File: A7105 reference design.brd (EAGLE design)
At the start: 14.7 x 11.8 mm, 38 parts, among them J1 JST-SH-3, SW1 BUTTON, U1 A7105, U2 ATTINY167, U3 NMOS, X1 ECX-2236

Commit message: Finished integrated rev 0.2
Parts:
- removed J1: JST-SH-3, nikdavis:JST-SH-3
- removed U$3, U$4: TESTPAD, AlienWhoop:TESTPAD
- added C19: 1uF, Perfect_0402:0402
- added U$10, U$11, U$12, U$6, U$7, U$8, U$9: TESTPAD, AlienWhoop:TESTPAD
- U3: value NMOS -> NMOSSOT833B/1006; device nikdavis:SOT23-3 -> nikdavis:SOT833B/DFN1006B-3
- moved R6 109.7 mm to (9.56, 3.17), flipped to the bottom, turned to 270 degrees
- moved C18 106.0 mm to (5.71, 7.90), flipped to the bottom
- moved R4 9.19 mm to (11.5, 10.7), turned to 180 degrees
- moved U3 3.90 mm to (14.0, 3.89)
- moved C11 2.54 mm to (8.87, 1.52), turned to 270 degrees
- moved R2 2.24 mm to (11.5, 5.47), turned to 90 degrees
- moved R3 2.10 mm to (9.92, 1.52), flipped to the top
- moved C1 1.95 mm to (5.66, 3.12), turned to 0 degrees
- moved SW1 1.86 mm to (11.0, 7.02), turned to 90 degrees
- moved C6 1.82 mm to (5.71, 4.02), turned to 0 degrees
- moved C10 1.64 mm to (4.95, 1.50), turned to 90 degrees
- moved U$5 1.00 mm to (7.24, 9.86)
- moved U2 1.00 mm to (10.4, 6.80)
- moved X1 0.64 mm to (5.46, 0.36)
- moved C14 0.58 mm to (0.85, 8.69)
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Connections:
- new net GPIO1: U1.16, U2.29
- net G: now also U3.P$1; no longer U3.1
- net GND: now also C19.2, U$9.TP, U3.P$2; no longer J1.2, J1.GND1, J1.GND2, U$4.TP, U3.2
- net MOSI: now also U$12.TP
- net RESET: now also U$7.TP
- net SBUS: now also U$6.TP, U3.P$3; no longer J1.3, U3.3
- net SCK: now also U$10.TP
- net SDIO: now also U$11.TP
- net VCC: now also C19.1, U$8.TP; no longer J1.1, U$3.TP
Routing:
- net SBUS_NONINV: track 11.7 -> 1.66 mm, vias 2 -> 0
- net G: track 1.30 -> 10.2 mm
- net SDIO: track 19.6 -> 11.6 mm
- net GPIO1: track 0.00 -> 7.85 mm, vias 0 -> 1
- net RESET: track 0.00 -> 6.47 mm, vias 0 -> 1
- net MOSI: track 1.15 -> 6.55 mm
- net GND: track 14.3 -> 10.6 mm, vias 18 -> 22
- net SCK: track 6.85 -> 10.2 mm
- net N$4: track 1.41 -> 3.94 mm
- net BIND: track 2.61 -> 4.94 mm
- net VCCA: track 13.2 -> 15.0 mm
- net AVRCLK: track 4.58 -> 3.30 mm
- net N$10: track 5.38 -> 4.27 mm
- net N$8: track 2.90 -> 3.96 mm
- net SCS: track 5.79 -> 4.91 mm
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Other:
- board size 14.7 x 11.8 mm -> 15 x 11.5 mm

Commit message: Cleanup before order
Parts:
- moved R5 0.56 mm to (7.65, 10.4)
- moved U$5 0.53 mm to (7.24, 10.4)
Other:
- board text added: "3.3"
- board text added: "G"
- board text added: "MI"
- board text added: "MO"
- board text added: "RST"
- board text added: "SB"
- board text added: "SCK"
- board text added: "uFlSky SBUS @nivvis V0.2"
- board text removed: "A7105 Ref Integrated V0.1 / 2019-02-16 nivvis"
- board text removed: "GND"
- board text removed: "VCC"

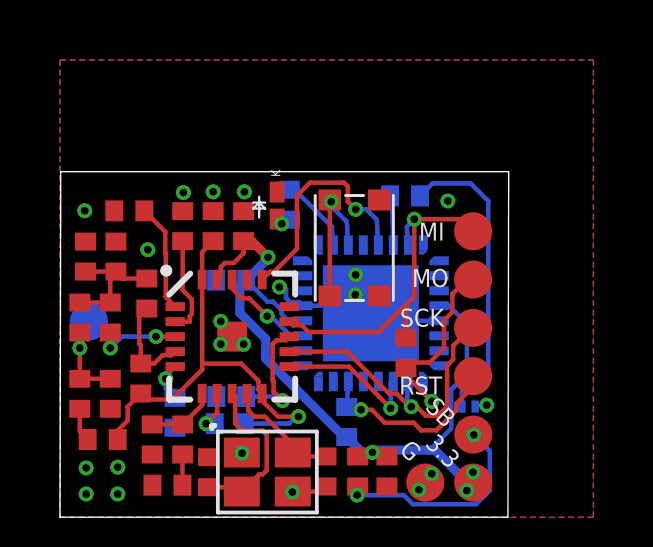
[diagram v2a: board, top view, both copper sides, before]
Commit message: Add bind pull up
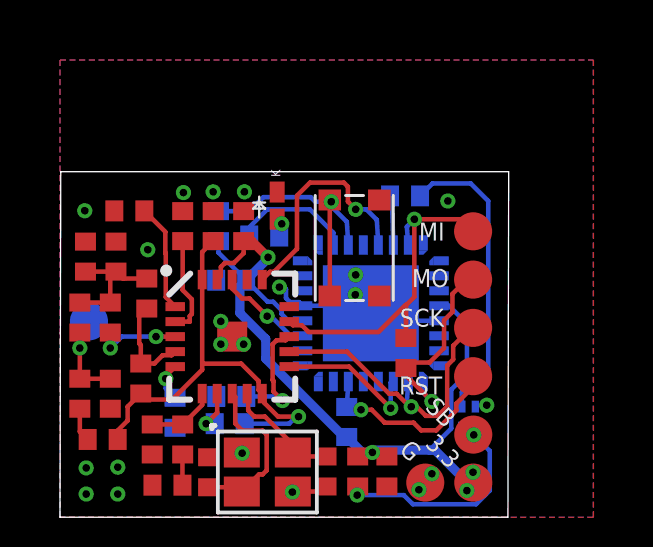
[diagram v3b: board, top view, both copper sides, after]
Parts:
- added R7: 10k, Perfect_0402:0402
- moved R5 1.34 mm to (6.81, 9.37), turned to 180 degrees
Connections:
- net BIND: now also R7.1
- net VCC: now also R7.2
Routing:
- net BIND: track 4.94 -> 8.95 mm
- net VCC: track 26.4 -> 28.0 mm
- net STATUS: track 2.54 -> 4.07 mm
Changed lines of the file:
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@@
 <setting verticaltext="up"/>
 </settings>
-<grid distance="0.001" unitdist="inch" unit="mm" style="lines" multiple="1" display="no" altdistance="5" altunitdist="mil" altunit="mil"/>
+<grid distance="0.001" unitdist="inch" unit="inch" style="lines" multiple="1" display="no" altdistance="5" altunitdist="mil" altunit="mil"/>
 <layers>
 <layer number="1" name="Top" color="4" fill="1" visible="yes" active="yes"/>
-<layer number="16" name="Bottom" color="1" fill="1" visible="no" active="yes"/>
-<layer number="17" name="Pads" color="2" fill="1" visible="no" active="yes"/>
-<layer number="18" name="Vias" color="2" fill="1" visible="no" active="yes"/>
-<layer number="19" name="Unrouted" color="6" fill="1" visible="no" active="yes"/>
-<layer number="20" name="Dimension" color="24" fill="1" visible="no" active="yes"/>
+<layer number="16" name="Bottom" color="1" fill="1" visible="yes" active="yes"/>
+<layer number="17" name="Pads" color="2" fill="1" visible="yes" active="yes"/>
+<layer number="18" name="Vias" color="2" fill="1" visible="yes" active="yes"/>
+<layer number="19" name="Unrouted" color="6" fill="1" visible="yes" active="yes"/>
+<layer number="20" name="Dimension" color="24" fill="1" visible="yes" active="yes"/>
 <layer number="21" name="tPlace" color="7" fill="1" visible="yes" active="yes"/>
-<layer number="22" name="bPlace" color="7" fill="1" visible="no" active="yes"/>
-<layer number="23" name="tOrigins" color="15" fill="1" visible="no" active="yes"/>
-<layer number="24" name="bOrigins" color="15" fill="1" visible="no" active="yes"/>
+<layer number="22" name="bPlace" color="7" fill="1" visible="yes" active="yes"/>
+<layer number="23" name="tOrigins" color="15" fill="1" visible="yes" active="yes"/>
+<layer number="24" name="bOrigins" color="15" fill="1" visible="yes" active="yes"/>
 <layer number="25" name="tNames" color="7" fill="1" visible="no" active="yes"/>
 <layer number="26" name="bNames" color="7" fill="1" visible="no" active="yes"/>
@@
 <element name="R4" library="Perfect_0402" package="0402" value="10k" x="11.5018" y="10.7102" smashed="yes" rot="MR180"/>
 <element name="SW1" library="nikdavis" package="PTS-830-SMD-SWITCH" value="BUTTON" x="11.0174" y="7.0238" smashed="yes" rot="R90"/>
-<element name="R5" library="Perfect_0402" package="0402" value="200" x="7.6454" y="10.414" smashed="yes" rot="MR270"/>
+<element name="R5" library="Perfect_0402" package="0402" value="200" x="6.8072" y="9.3726" smashed="yes" rot="MR180"/>
 <element name="U$5" library="alienflight" package="0402LED" value="SMD-CHIP-LED-0402" x="7.239" y="10.3886" smashed="yes" rot="R270"/>
 <element name="C18" library="Perfect_0402" package="0402" value="10nF" x="5.7052" y="7.8982" smashed="yes" rot="MR0">
@@
 <attribute name="DNP" value="T" x="13.77" y="7.92" size="1.778" layer="27" display="off"/>
 <attribute name="VALUE" x="13.135" y="7.158" size="0.0254" layer="27"/>
+</element>
+<element name="R7" library="Perfect_0402" package="0402" value="10k" x="5.2832" y="9.7028" smashed="yes" rot="MR270">
+<attribute name="NAME" x="4.7482" y="10.3378" size="0.8128" layer="26" ratio="10" rot="MR270"/>
+<attribute name="VALUE" x="6.6882" y="10.3378" size="0.8128" layer="28" ratio="10" rot="MR270"/>
 </element>
 </elements>
@@
 <wire x1="13.7754" y1="1.1532" x2="13.7754" y2="1.49" width="0.3048" layer="1"/>
 <wire x1="13.7754" y1="1.49" x2="13.7668" y2="1.4986" width="0.3048" layer="1"/>
+<contactref element="R7" pad="2"/>
+<wire x1="5.2832" y1="9.2028" x2="5.2832" y2="8.8202" width="0.1524" layer="16"/>
+<wire x1="5.2832" y1="8.8202" x2="6.2052" y2="7.8982" width="0.1524" layer="16"/>
 </signal>
 <signal name="N$8">
@@
 <wire x1="9.0424" y1="10.5238" x2="9.0424" y2="10.5156" width="0.1524" layer="1"/>
 <wire x1="8.9924" y1="10.5738" x2="8.9924" y2="7.3738" width="0.1524" layer="1"/>
+<contactref element="R7" pad="1"/>
+<wire x1="9.0424" y1="10.5156" x2="8.50825625" y2="10.5156" width="0.1524" layer="16"/>
+<wire x1="8.50825625" y1="10.5156" x2="8.35585625" y2="10.668" width="0.1524" layer="16"/>
+<wire x1="8.35585625" y1="10.668" x2="6.7818" y2="10.668" width="0.1524" layer="16"/>
+<wire x1="6.7818" y1="10.668" x2="6.3166" y2="10.2028" width="0.1524" layer="16"/>
+<wire x1="6.3166" y1="10.2028" x2="5.2832" y2="10.2028" width="0.1524" layer="16"/>
 </signal>
 <signal name="RESET">
@@
 <contactref element="U2" pad="26"/>
 <contactref element="R5" pad="1"/>
-<wire x1="9.1116" y1="9.0726" x2="9.0608" y2="9.6804" width="0.1524" layer="16"/>
-<wire x1="9.0608" y1="9.6804" x2="7.8272" y2="10.914" width="0.1524" layer="16"/>
-<wire x1="7.8272" y1="10.914" x2="7.6454" y2="10.914" width="0.1524" layer="16"/>
+<wire x1="9.1116" y1="9.0726" x2="9.1116" y2="9.4812" width="0.1524" layer="16"/>
+<wire x1="8.3312" y1="10.2616" x2="6.9088" y2="10.2616" width="0.1524" layer="16"/>
+<wire x1="6.9088" y1="10.2616" x2="6.3072" y2="9.66" width="0.1524" layer="16"/>
+<wire x1="6.3072" y1="9.66" x2="6.3072" y2="9.3726" width="0.1524" layer="16"/>
+<wire x1="9.1116" y1="9.4812" x2="8.3312" y2="10.2616" width="0.1524" layer="16"/>
 </signal>
 <signal name="N$9">
@@
 <contactref element="U$5" pad="2"/>
 <via x="7.3914" y="9.779" extent="1-16" drill="0.254"/>
-<wire x1="7.6454" y1="9.914" x2="7.5104" y2="9.779" width="0.1524" layer="16"/>
-<wire x1="7.3914" y1="9.779" x2="7.5104" y2="9.779" width="0.1524" layer="16"/>
+<wire x1="7.3914" y1="9.779" x2="7.3072" y2="9.6948" width="0.1524" layer="16"/>
+<wire x1="7.3072" y1="9.6948" x2="7.3072" y2="9.3726" width="0.1524" layer="16"/>
 <wire x1="7.239" y1="9.9386" x2="7.3914" y2="9.7862" width="0.1524" layer="1"/>
 <wire x1="7.3914" y1="9.7862" x2="7.3914" y2="9.779" width="0.1524" layer="1"/>

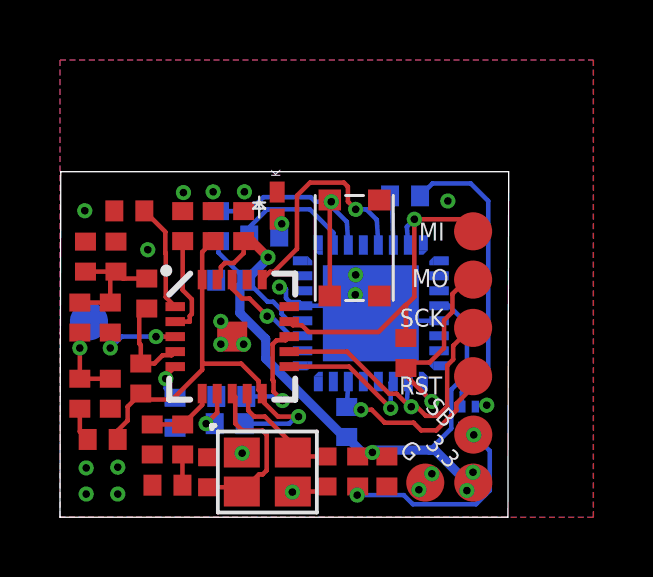
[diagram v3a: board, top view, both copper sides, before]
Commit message: Start STM rehaul -- stuck on EEPROM decision
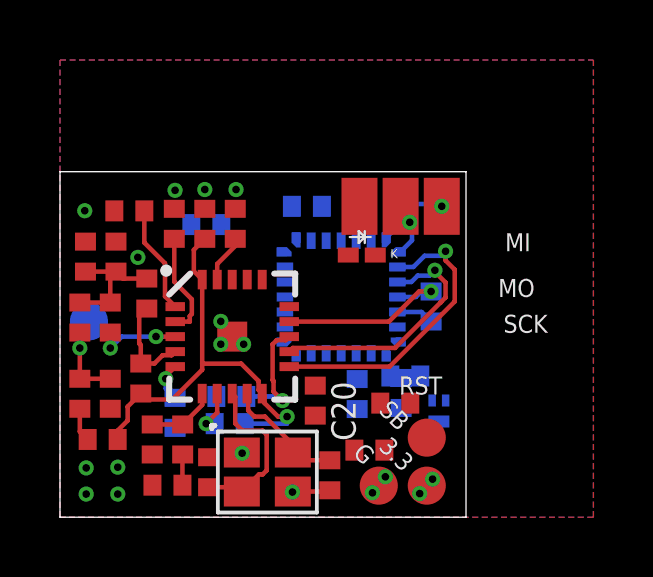
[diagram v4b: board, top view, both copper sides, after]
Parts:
- removed R7: 10k, Perfect_0402:0402
- removed SW1: BUTTON, nikdavis:PTS-830-SMD-SWITCH
- removed U$10, U$11, U$12, U$7: TESTPAD, AlienWhoop:TESTPAD
- added C20, C21: 10nF, Perfect_0402:0402
- added TP1, TP2, TP3: TESTPAD, nikdavis:SMTPAD-RECT
- R6: value 4k7 -> 10k
- U2: value ATTINY167 -> STM32F031G4U6; device nikdavis:VQFN-32 -> STM32F031G4U6:QFN50P400X400X60-28N
- moved R4 6.00 mm to (11.5, 4.71), turned to 0 degrees
- moved C18 5.66 mm to (9.91, 4.11), turned to 270 degrees
- moved U$5 3.27 mm to (10.1, 8.74), turned to 180 degrees
- moved R3 2.60 mm to (11.2, 3.80), turned to 180 degrees
- moved R6 2.06 mm to (11.4, 4.14), turned to 90 degrees
- moved R5 1.97 mm to (4.88, 9.75)
- moved R2 1.76 mm to (12.4, 7.02), flipped to the bottom
- moved U$9 1.55 mm to (10.6, 1.05)
- moved U$6 1.55 mm to (12.2, 2.65)
- moved U$8 1.55 mm to (12.2, 1.05)
- moved U2 1.13 mm to (9.37, 7.34), turned to 90 degrees
- moved U3 1.01 mm to (13.0, 4.09)
- moved C19 0.92 mm to (10.3, 2.24), turned to 180 degrees
- moved C5 0.29 mm to (4.83, 9.78)
- moved C9 0.29 mm to (5.84, 9.78)
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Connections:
- removed net AVRCLK: U1.18, U2.19
- removed net BIND: R7.1, SW1.P$1, SW1.P$2, U2.27
- removed net RESET: R6.1, U$7.TP, U2.14
- removed net SBUS_NONINV: R4.1, U2.30
- new net MCUCLK: U1.18
- new net N$11: C18.1, U2.4
- new net N$5: R6.2, U2.1
- new net NSBUS: R4.1, U2.27
- new net SWCLK: TP2.P$1, U2.22
- new net SWD: TP1.P$1, U2.21
- net GND: now also C20.2, C21.2, R6.1, TP3.P$1, U2.16; no longer SW1.P$3, SW1.P$4, U2.21, U2.5, U2.PAD
- net GPIO1: now also U2.20; no longer U2.29
- net MOSI: now also U2.26; no longer U$12.TP, U2.9
- net SCK: now also U2.24; no longer U$10.TP, U2.10
- net SCS: now also U2.23; no longer U2.11
- net SDIO: now also U2.25; no longer U$11.TP, U2.31
- net STATUS: no longer U2.26
- net VCC: now also C20.1, C21.1, U2.17, U2.5; no longer C18.1, R6.2, R7.2, U2.20, U2.4
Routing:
- net VCC: track 28.0 -> 1.61 mm, vias 4 -> 0
- net G: track 10.2 -> 0.00 mm
- net BIND: track 8.95 -> 0.00 mm, vias 1 -> 0
- net GPIO1: track 7.85 -> 0.00 mm, vias 1 -> 0
- net SBUS: track 7.44 -> 0.00 mm, vias 2 -> 0
- net GND: track 10.6 -> 3.82 mm, vias 22 -> 17
- net RESET: track 6.47 -> 0.00 mm, vias 1 -> 0
- net MOSI: track 6.55 -> 1.25 mm, vias 1 -> 0
- net SDIO: track 11.6 -> 6.34 mm
- net SCS: track 4.91 -> 10.0 mm
- net STATUS: track 4.07 -> 0.00 mm
- net AVRCLK: track 3.30 -> 0.00 mm, vias 1 -> 0
- net SWD: track 0.00 -> 2.62 mm, vias 0 -> 1
- net SWCLK: track 0.00 -> 1.86 mm, vias 0 -> 1
- net SCK: track 10.2 -> 8.43 mm
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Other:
- board size 15 x 11.5 mm -> 13.5 x 11.5 mm

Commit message: Small edits
Bit of board prep organization. Small schematic clean up and notes.
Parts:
- removed C21: 10nF, Perfect_0402:0402
- C20: value 10nF -> 0.1uF
- moved C20 6.32 mm to (7.98, 10.2), flipped to the bottom, turned to 0 degrees
- moved U$5 2.74 mm to (7.80, 10.3)
- moved R4 1.00 mm to (12.4, 5.22), turned to 270 degrees
- moved R5 0.84 mm to (5.64, 10.1)
- moved R3 0.47 mm to (10.8, 3.56), turned to 270 degrees
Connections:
- net GND: no longer C21.2
- net VCC: no longer C21.1

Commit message: First steps
Remove inverter
Make todo list
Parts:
- removed R3, R4: 10k, Perfect_0402:0402
- removed U3: NMOSSOT833B/1006, nikdavis:SOT833B/DFN1006B-3
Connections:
- removed net G: R4.2, U3.P$1
- removed net NSBUS: R4.1, U2.27
- net GND: no longer U3.P$2
- net SBUS: now also U2.27; no longer R3.1, U3.P$3
- net VCC: no longer R3.2
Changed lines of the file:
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@@
 <element name="X1" library="nikdavis" package="2.5X2.0MM_CRYSTAL" value="ECX-2236" x="5.461" y="0.3556" smashed="yes"/>
 <element name="R2" library="Perfect_0402" package="0402" value="10k" x="12.3694" y="7.0248" smashed="yes" rot="MR90"/>
-<element name="R3" library="Perfect_0402" package="0402" value="10k" x="10.7774" y="3.556" smashed="yes" rot="R270"/>
-<element name="R4" library="Perfect_0402" package="0402" value="10k" x="12.3742" y="5.2156" smashed="yes" rot="MR270"/>
 <element name="R5" library="Perfect_0402" package="0402" value="200" x="5.6388" y="10.1092" smashed="yes" rot="MR180"/>
 <element name="U$5" library="alienflight" package="0402LED" value="SMD-CHIP-LED-0402" x="7.7978" y="10.287" smashed="yes" rot="R180"/>
@@
 <attribute name="VALUE" x="9.991" y="0.2896" size="0.0254" layer="27"/>
 </element>
-<element name="U3" library="nikdavis" package="SOT833B/DFN1006B-3" value="NMOSSOT833B/1006" x="12.9794" y="4.0894" smashed="yes" rot="MR270"/>
 <element name="C19" library="Perfect_0402" package="0402" value="1uF" x="10.3124" y="2.2352" smashed="yes" rot="R180"/>
 <element name="U2" library="STM32F031G4U6" package="QFN50P400X400X60-28N" value="STM32F031G4U6" x="9.3726" y="7.3406" smashed="yes" rot="MR90">
@@
 <wire x1="0.6604" y1="2.8528" x2="0.6604" y2="3.6148" width="0.1524" layer="1"/>
 <contactref element="U$5" pad="1"/>
-<contactref element="U3" pad="P$2"/>
 <contactref element="U$9" pad="TP"/>
 <contactref element="C19" pad="2"/>
@@
 <contactref element="C20" pad="2"/>
 <contactref element="TP3" pad="P$1"/>
+<wire x1="7.4756" y1="10.1854" x2="8.2478" y2="10.287" width="0" layer="19" extent="1-16"/>
+<wire x1="8.3726" y1="9.2156" x2="8.2478" y2="10.287" width="0" layer="19" extent="1-16"/>
+<wire x1="5.842" y1="10.279" x2="7.4756" y2="10.1854" width="0" layer="19" extent="1-16"/>
+<wire x1="5.8674" y1="10.922" x2="5.842" y2="10.279" width="0" layer="19" extent="1-1"/>
+<wire x1="4.826" y1="10.279" x2="5.842" y2="10.279" width="0" layer="19" extent="1-1"/>
+<wire x1="4.826" y1="10.922" x2="4.826" y2="10.279" width="0" layer="19" extent="1-1"/>
+<wire x1="3.8354" y1="10.8966" x2="4.826" y2="10.922" width="0" layer="19" extent="1-1"/>
+<wire x1="3.81" y1="10.279" x2="3.8354" y2="10.8966" width="0" layer="19" extent="1-1"/>
 <wire x1="9.9822" y1="10.3632" x2="8.2478" y2="10.287" width="0" layer="19" extent="1-1"/>
-<wire x1="8.3726" y1="9.2156" x2="9.9822" y2="10.3632" width="0" layer="19" extent="1-16"/>
+<wire x1="1.8114" y1="10.2108" x2="3.81" y2="10.279" width="0" layer="19" extent="1-1"/>
+<wire x1="0.8254" y1="10.2158" x2="1.8114" y2="10.2108" width="0" layer="19" extent="1-1"/>
+<wire x1="1.8654" y1="9.1868" x2="1.8114" y2="10.2108" width="0" layer="19" extent="1-1"/>
+<wire x1="2.5952" y1="8.6618" x2="1.8654" y2="9.1868" width="0" layer="19" extent="1-1"/>
+<wire x1="0.8494" y1="9.1868" x2="1.8654" y2="9.1868" width="0" layer="19" extent="1-1"/>
 <wire x1="7.6404" y1="7.0198" x2="8.3726" y2="9.2156" width="0" layer="19" extent="1-16"/>
 <wire x1="6.1214" y1="5.7658" x2="7.6404" y2="7.0198" width="0" layer="19" extent="1-1"/>
@@
 <wire x1="9.8124" y1="2.2352" x2="10.8458" y2="1.3462" width="0" layer="19" extent="1-1"/>
 <wire x1="9.9072" y1="3.605" x2="9.8124" y2="2.2352" width="0" layer="19" extent="1-16"/>
-<wire x1="7.4756" y1="10.1854" x2="9.9072" y2="3.605" width="0" layer="19" extent="1-16"/>
 <wire x1="11.373" y1="3.641" x2="9.9072" y2="3.605" width="0" layer="19" extent="16-16"/>
-<wire x1="12.8544" y1="3.8894" x2="11.373" y2="3.641" width="0" layer="19" extent="16-16"/>
-<wire x1="5.842" y1="10.279" x2="8.3726" y2="9.2156" width="0" layer="19" extent="1-16"/>
-<wire x1="5.8674" y1="10.922" x2="5.842" y2="10.279" width="0" layer="19" extent="1-1"/>
-<wire x1="4.826" y1="10.279" x2="5.842" y2="10.279" width="0" layer="19" extent="1-1"/>
-<wire x1="4.826" y1="10.922" x2="4.826" y2="10.279" width="0" layer="19" extent="1-1"/>
-<wire x1="3.8354" y1="10.8966" x2="4.826" y2="10.922" width="0" layer="19" extent="1-1"/>
-<wire x1="3.81" y1="10.279" x2="3.8354" y2="10.8966" width="0" layer="19" extent="1-1"/>
-<wire x1="1.8114" y1="10.2108" x2="3.81" y2="10.279" width="0" layer="19" extent="1-1"/>
-<wire x1="0.8254" y1="10.2158" x2="1.8114" y2="10.2108" width="0" layer="19" extent="1-1"/>
-<wire x1="1.8654" y1="9.1868" x2="1.8114" y2="10.2108" width="0" layer="19" extent="1-1"/>
-<wire x1="2.5952" y1="8.6618" x2="1.8654" y2="9.1868" width="0" layer="19" extent="1-1"/>
-<wire x1="0.8494" y1="9.1868" x2="1.8654" y2="9.1868" width="0" layer="19" extent="1-1"/>
 </signal>
 <signal name="N$1">
@@
 <contactref element="U1" pad="19"/>
 <contactref element="C9" pad="1"/>
-<contactref element="R3" pad="2"/>
-<contactref element="U$8" pad="TP"/>
-<contactref element="C19" pad="1"/>
 <contactref element="C20" pad="1"/>
 <contactref element="U2" pad="17"/>
@@
 <wire x1="5.842" y1="9.0424" x2="5.842" y2="9.279" width="0.1524" layer="1"/>
 <wire x1="5.2404" y1="8.4408" x2="5.842" y2="9.0424" width="0.1524" layer="1"/>
-<wire x1="5.842" y1="9.279" x2="8.8726" y2="9.2156" width="0" layer="19" extent="1-16"/>
+<contactref element="U$8" pad="TP"/>
+<contactref element="C19" pad="1"/>
+<wire x1="8.8726" y1="9.2156" x2="8.4756" y2="10.1854" width="0" layer="19" extent="16-16"/>
+<wire x1="5.842" y1="9.279" x2="8.4756" y2="10.1854" width="0" layer="19" extent="1-16"/>
 <wire x1="8.8726" y1="5.4656" x2="8.8726" y2="9.2156" width="0" layer="19" extent="16-16"/>
-<wire x1="8.4756" y1="10.1854" x2="8.8726" y2="5.4656" width="0" layer="19" extent="1-16"/>
-<wire x1="10.7774" y1="3.056" x2="8.4756" y2="10.1854" width="0" layer="19" extent="1-1"/>
-<wire x1="10.8124" y1="2.2352" x2="10.7774" y2="3.056" width="0" layer="19" extent="1-1"/>
+<wire x1="10.8124" y1="2.2352" x2="8.8726" y2="5.4656" width="0" layer="19" extent="1-16"/>
 <wire x1="12.226" y1="1.0516" x2="10.8124" y2="2.2352" width="0" layer="19" extent="1-1"/>
 </signal>
@@
 <wire x1="12.0536" y1="6.8406" x2="11.2476" y2="6.8406" width="0.1524" layer="16"/>
 </signal>
-<signal name="NSBUS">
-<contactref element="R4" pad="1"/>
+<signal name="SBUS">
+<contactref element="U$6" pad="TP"/>
 <contactref element="U2" pad="27"/>
-<wire x1="11.2476" y1="6.3406" x2="12.3742" y2="5.7156" width="0" layer="19" extent="16-16"/>
-</signal>
-<signal name="SBUS">
-<contactref element="R3" pad="1"/>
-<contactref element="U$6" pad="TP"/>
-<contactref element="U3" pad="P$3"/>
-<wire x1="12.6294" y1="3.1894" x2="12.226" y2="2.6516" width="0" layer="19" extent="1-16"/>
-<wire x1="10.7774" y1="4.056" x2="12.6294" y2="3.1894" width="0" layer="19" extent="1-16"/>
-</signal>
-<signal name="G">
-<contactref element="R4" pad="2"/>
-<contactref element="U3" pad="P$1"/>
-<wire x1="12.4044" y1="3.8894" x2="12.3742" y2="4.7156" width="0" layer="19" extent="16-16"/>
+<wire x1="12.226" y1="2.6516" x2="11.2476" y2="6.3406" width="0" layer="19" extent="1-16"/>
 </signal>
 <signal name="STATUS">
